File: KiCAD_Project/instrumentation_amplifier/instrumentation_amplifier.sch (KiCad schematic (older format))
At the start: 29 parts, among them CON1 1-0000001, J1 1-0000120, J2 Jumper, J3 Jumper, J4 1-0000120, SW1 1-0000852, U1 1-0000801, U2 1-0000465

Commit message: Production ready Rev 1.0
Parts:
- added J5: NP_Conn_01x04, np_connectors:PinHeader_1x04_P2.54mm_Vertical, symbol np_connectors:NP_Conn_01x04
- added PCB1: barepcb, misc:barepcb, symbol misc:barepcb
- FID1, FID2: footprint Fiducial:Fiducial_0.5mm_Mask1.5mm -> mechanical:Fiducial_1mm_Mask2mm; symbol Mechanical:Fiducial -> mechanical:Fiducial_1mm_2mm; Internal Part Number (none) -> 0-0000000; PValue (none) -> Fiducial; Populated (none) -> 0
- H1, H2, H3, H4: footprint MountingHole:MountingHole_2.1mm -> mechanical:MountingHole_3.2mm_M3_ISO7380; symbol Mechanical:MountingHole -> mechanical:M3_ISO_7380; Internal Part Number (none) -> 0-0000000; PValue (none) -> M3; Populated (none) -> 0
- J1: footprint capacitors_1206:1-0000191 -> connectors:1-0000120
- J2, J3: Internal Part Number (none) -> 0-0000000; Populated (none) -> 0
- R6: PValue 0R0 -> NP; Populated NP -> 0
- U1: symbol instrumentation_amplifier-rescue:1-0000801-amplifiers -> amplifiers:1-0000801
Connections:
- wire segments 80 -> 84
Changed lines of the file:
@@
 encoding utf-8
 Sheet 1 1
-Title "GEARS Instrumentation Amplifier"
-Date "2021-04-14"
+Title "Instrumentation Amplifier Demo"
+Date "2021-04-21"
 Rev "1.0"
 Comp "Leeman Geophysical LLC"
@@
 $EndComp
 $Comp
-L instrumentation_amplifier-rescue:1-0000801-amplifiers U1
+L amplifiers:1-0000801 U1
 U 1 1 60778415
 P 6700 3825
@@
 F 3 "~" H 4550 4450 50  0001 C CNN
 F 4 "1-0000006" H 4550 4450 50  0001 C CNN "Internal Part Number"
-F 5 "NP" H 4550 4450 50  0001 C CNN "Populated"
-F 6 "0R0" V 4550 4375 50  0000 L CNN "PValue"
+F 5 "0" H 4550 4450 50  0001 C CNN "Populated"
+F 6 "NP" V 4550 4400 50  0000 L CNN "PValue"
 	1    4550 4450
 	1    0    0    -1
@@
 F 0 "J1" H 3875 3675 50  0000 C CNN
 F 1 "1-0000120" H 3875 3675 50  0001 C CNN
-F 2 "capacitors_1206:1-0000191" H 3875 3875 50  0001 C CNN
+F 2 "connectors:1-0000120" H 3875 3875 50  0001 C CNN
 F 3 "~" H 3875 3875 50  0001 C CNN
 F 4 "1-0000120" H 3875 3875 50  0001 C CNN "Internal Part Number"
 F 5 "1" H 3875 3875 50  0001 C CNN "Populated"
-F 6 "TSW-102-07-T-S" H 3875 3575 50  0000 C CNN "PValue"
+F 6 "TSW-102-07-T-S" H 3875 3575 50  0001 C CNN "PValue"
 	1    3875 3875
 	-1   0    0    1
@@
 F 4 "1-0000120" H 8475 3825 50  0001 C CNN "Internal Part Number"
 F 5 "1" H 8475 3825 50  0001 C CNN "Populated"
-F 6 "TSW-102-07-T-S" H 8475 4025 50  0000 C CNN "PValue"
+F 6 "TSW-102-07-T-S" H 8475 4025 50  0001 C CNN "PValue"
 	1    8475 3825
 	1    0    0    -1
@@
 U 1 1 607ABDFA
 P 4425 2600
-F 0 "J3" V 4429 2680 50  0000 L CNN
-F 1 "Jumper" V 4520 2680 50  0000 L CNN
+F 0 "J3" V 4425 2325 50  0000 L CNN
+F 1 "Jumper" V 4525 2150 50  0000 L CNN
 F 2 "Connector_PinHeader_2.54mm:PinHeader_2x02_P2.54mm_Vertical" H 4425 2600 50  0001 C CNN
 F 3 "~" H 4425 2600 50  0001 C CNN
+F 4 "0-0000000" H 4425 2600 50  0001 C CNN "Internal Part Number"
+F 5 "0" H 4425 2600 50  0001 C CNN "Populated"
 	1    4425 2600
 	0    1    1    0
@@
 F 2 "Connector_PinHeader_2.54mm:PinHeader_2x02_P2.54mm_Vertical" H 4325 5125 50  0001 C CNN
 F 3 "~" H 4325 5125 50  0001 C CNN
+F 4 "0-0000000" H 4325 5125 50  0001 C CNN "Internal Part Number"
+F 5 "0" H 4325 5125 50  0001 C CNN "Populated"
 	1    4325 5125
 	0    -1   -1   0
@@
 $EndComp
 $Comp
-L Mechanical:MountingHole H1
+L mechanical:M3_ISO_7380 H1
 U 1 1 60869A6E
 P 700 6825
 F 0 "H1" H 800 6871 50  0000 L CNN
 F 1 "MountingHole" H 800 6780 50  0000 L CNN
-F 2 "MountingHole:MountingHole_2.1mm" H 700 6825 50  0001 C CNN
-F 3 "~" H 700 6825 50  0001 C CNN
+F 2 "mechanical:MountingHole_3.2mm_M3_ISO7380" H 700 6825 50  0001 C CNN
+F 3 "None" H 700 6825 50  0001 C CNN
+F 4 "0-0000000" H 700 6825 50  0001 C CNN "Internal Part Number"
+F 5 "0" H 700 6825 50  0001 C CNN "Populated"
+F 6 "M3" H 700 6825 50  0001 C CNN "PValue"
 	1    700  6825
 	1    0    0    -1
 $EndComp
 $Comp
-L Mechanical:MountingHole H2
+L mechanical:M3_ISO_7380 H2
 U 1 1 6086A8C6
 P 700 7075
 F 0 "H2" H 800 7121 50  0000 L CNN
 F 1 "MountingHole" H 800 7030 50  0000 L CNN
-F 2 "MountingHole:MountingHole_2.1mm" H 700 7075 50  0001 C CNN
-F 3 "~" H 700 7075 50  0001 C CNN
+F 2 "mechanical:MountingHole_3.2mm_M3_ISO7380" H 700 7075 50  0001 C CNN
+F 3 "None" H 700 7075 50  0001 C CNN
+F 4 "0-0000000" H 700 7075 50  0001 C CNN "Internal Part Number"
+F 5 "0" H 700 7075 50  0001 C CNN "Populated"
+F 6 "M3" H 700 7075 50  0001 C CNN "PValue"
 	1    700  7075
 	1    0    0    -1
 $EndComp
 $Comp
-L Mechanical:MountingHole H3
+L mechanical:M3_ISO_7380 H3
 U 1 1 6086B2CF
 P 700 7325
 F 0 "H3" H 800 7371 50  0000 L CNN
 F 1 "MountingHole" H 800 7280 50  0000 L CNN
-F 2 "MountingHole:MountingHole_2.1mm" H 700 7325 50  0001 C CNN
-F 3 "~" H 700 7325 50  0001 C CNN
+F 2 "mechanical:MountingHole_3.2mm_M3_ISO7380" H 700 7325 50  0001 C CNN
+F 3 "None" H 700 7325 50  0001 C CNN
+F 4 "0-0000000" H 700 7325 50  0001 C CNN "Internal Part Number"
+F 5 "0" H 700 7325 50  0001 C CNN "Populated"
+F 6 "M3" H 700 7325 50  0001 C CNN "PValue"
 	1    700  7325
 	1    0    0    -1
 $EndComp
 $Comp
-L Mechanical:MountingHole H4
+L mechanical:M3_ISO_7380 H4
 U 1 1 6086D5E1
 P 700 7575
 F 0 "H4" H 800 7621 50  0000 L CNN
 F 1 "MountingHole" H 800 7530 50  0000 L CNN
-F 2 "MountingHole:MountingHole_2.1mm" H 700 7575 50  0001 C CNN
-F 3 "~" H 700 7575 50  0001 C CNN
+F 2 "mechanical:MountingHole_3.2mm_M3_ISO7380" H 700 7575 50  0001 C CNN
+F 3 "None" H 700 7575 50  0001 C CNN
+F 4 "0-0000000" H 700 7575 50  0001 C CNN "Internal Part Number"
+F 5 "0" H 700 7575 50  0001 C CNN "Populated"
+F 6 "M3" H 700 7575 50  0001 C CNN "PValue"
 	1    700  7575
 	1    0    0    -1
@@
 	6700 2750 6700 3125
 $Comp
-L Mechanical:Fiducial FID1
+L mechanical:Fiducial_1mm_2mm FID1
 U 1 1 607C3F0B
 P 1575 6825
 F 0 "FID1" H 1660 6871 50  0000 L CNN
 F 1 "Fiducial" H 1660 6780 50  0000 L CNN
-F 2 "Fiducial:Fiducial_0.5mm_Mask1.5mm" H 1575 6825 50  0001 C CNN
+F 2 "mechanical:Fiducial_1mm_Mask2mm" H 1575 6825 50  0001 C CNN
 F 3 "~" H 1575 6825 50  0001 C CNN
+F 4 "0-0000000" H 1575 6825 50  0001 C CNN "Internal Part Number"
+F 5 "0" H 1575 6825 50  0001 C CNN "Populated"
+F 6 "Fiducial" H 1575 6825 50  0001 C CNN "PValue"
 	1    1575 6825
 	1    0    0    -1
 $EndComp
 $Comp
-L Mechanical:Fiducial FID2
+L mechanical:Fiducial_1mm_2mm FID2
 U 1 1 607C4B56
 P 1575 7100
 F 0 "FID2" H 1660 7146 50  0000 L CNN
 F 1 "Fiducial" H 1660 7055 50  0000 L CNN
-F 2 "Fiducial:Fiducial_0.5mm_Mask1.5mm" H 1575 7100 50  0001 C CNN
+F 2 "mechanical:Fiducial_1mm_Mask2mm" H 1575 7100 50  0001 C CNN
 F 3 "~" H 1575 7100 50  0001 C CNN
+F 4 "0-0000000" H 1575 7100 50  0001 C CNN "Internal Part Number"
+F 5 "0" H 1575 7100 50  0001 C CNN "Populated"
+F 6 "Fiducial" H 1575 7100 50  0001 C CNN "PValue"
 	1    1575 7100
 	1    0    0    -1
 $EndComp
+$Comp
+L power:+5V #PWR0113
+U 1 1 60809472
+P -600 1300
+F 0 "#PWR0113" H -600 1150 50  0001 C CNN
+F 1 "+5V" H -585 1473 50  0000 C CNN
+F 2 "" H -600 1300 50  0001 C CNN
+F 3 "" H -600 1300 50  0001 C CNN
+	1    -600 1300
+	1    0    0    -1
+$EndComp
+$Comp
+L power:-5V #PWR0114
+U 1 1 608096D5
+P -950 1300
+F 0 "#PWR0114" H -950 1400 50  0001 C CNN
+F 1 "-5V" H -935 1473 50  0000 C CNN
+F 2 "" H -950 1300 50  0001 C CNN
+F 3 "" H -950 1300 50  0001 C CNN
+	1    -950 1300
+	-1   0    0    1
+$EndComp
+$Comp
+L power:GND #PWR0115
+U 1 1 60809941
+P -1350 1300
+F 0 "#PWR0115" H -1350 1050 50  0001 C CNN
+F 1 "GND" H -1345 1127 50  0000 C CNN
+F 2 "" H -1350 1300 50  0001 C CNN
+F 3 "" H -1350 1300 50  0001 C CNN
+	1    -1350 1300
+	1    0    0    -1
+$EndComp
+$Comp
+L power:PWR_FLAG #FLG0101
+U 1 1 60809C8F
+P -950 1300
+F 0 "#FLG0101" H -950 1375 50  0001 C CNN
+F 1 "PWR_FLAG" H -950 1473 50  0000 C CNN
+F 2 "" H -950 1300 50  0001 C CNN
+F 3 "~" H -950 1300 50  0001 C CNN
+	1    -950 1300
+	1    0    0    -1
+$EndComp
+$Comp
+L power:PWR_FLAG #FLG0102
+U 1 1 6080A993
+P -1350 1300
+F 0 "#FLG0102" H -1350 1375 50  0001 C CNN
+F 1 "PWR_FLAG" H -1350 1473 50  0000 C CNN
+F 2 "" H -1350 1300 50  0001 C CNN
+F 3 "~" H -1350 1300 50  0001 C CNN
+	1    -1350 1300
+	1    0    0    -1
+$EndComp
+$Comp
+L power:PWR_FLAG #FLG0103
+U 1 1 6080AF02
+P -600 1300
+F 0 "#FLG0103" H -600 1375 50  0001 C CNN
+F 1 "PWR_FLAG" H -600 1473 50  0000 C CNN
+F 2 "" H -600 1300 50  0001 C CNN
+F 3 "~" H -600 1300 50  0001 C CNN
+	1    -600 1300
+	-1   0    0    1
+$EndComp
+$Comp
+L misc:barepcb PCB1
+U 1 1 6081342E
+P 10600 6325
+F 0 "PCB1" H 10500 6375 50  0000 L CNN
+F 1 "barepcb" H 10450 6275 50  0000 L CNN
+F 2 "misc:barepcb" H 10600 6325 50  0001 C CNN
+F 3 "" H 10600 6325 50  0001 C CNN
+F 4 "3-0000082" H 10600 6325 50  0001 C CNN "Internal Part Number"
+F 5 "1" H 10600 6325 50  0001 C CNN "Populated"
+F 6 "Bare PCB" H 10600 6325 50  0001 C CNN "PValue"
+	1    10600 6325
+	1    0    0    -1
+$EndComp
+$Comp
+L np_connectors:NP_Conn_01x04 J5
+U 1 1 6081C83C
+P 2175 3875
+F 0 "J5" H 2255 3867 50  0000 L CNN
+F 1 "NP_Conn_01x04" H 2175 3575 50  0001 C CNN
+F 2 "np_connectors:PinHeader_1x04_P2.54mm_Vertical" H 2175 3875 50  0001 C CNN
+F 3 "~" H 2175 3875 50  0001 C CNN
+F 4 "0-0000000" H 2175 3875 50  0001 C CNN "Internal Part Number"
+F 5 "0" H 2175 3875 50  0001 C CNN "Populated"
+F 6 "Power" H 2255 3776 50  0000 L CNN "PValue"
+	1    2175 3875
+	1    0    0    -1
+$EndComp
+$Comp
+L power:-5V #PWR0116
+U 1 1 6081E16C
+P 1975 4075
+F 0 "#PWR0116" H 1975 4175 50  0001 C CNN
+F 1 "-5V" H 1990 4248 50  0000 C CNN
+F 2 "" H 1975 4075 50  0001 C CNN
+F 3 "" H 1975 4075 50  0001 C CNN
+	1    1975 4075
+	-1   0    0    1
+$EndComp
+$Comp
+L power:+5V #PWR0117
+U 1 1 6081E5EF
+P 1975 3775
+F 0 "#PWR0117" H 1975 3625 50  0001 C CNN
+F 1 "+5V" H 1990 3948 50  0000 C CNN
+F 2 "" H 1975 3775 50  0001 C CNN
+F 3 "" H 1975 3775 50  0001 C CNN
+	1    1975 3775
+	1    0    0    -1
+$EndComp
+$Comp
+L power:GND #PWR0118
+U 1 1 6081EBDE
+P 1725 4100
+F 0 "#PWR0118" H 1725 3850 50  0001 C CNN
+F 1 "GND" H 1730 3927 50  0000 C CNN
+F 2 "" H 1725 4100 50  0001 C CNN
+F 3 "" H 1725 4100 50  0001 C CNN
+	1    1725 4100
+	1    0    0    -1
+$EndComp
+Wire Wire Line
+	1725 4100 1725 3975
+Wire Wire Line
+	1725 3975 1975 3975
+Wire Wire Line
+	1975 3875 1725 3875
+Wire Wire Line
+	1725 3875 1725 3975
+Connection ~ 1725 3975
 $EndSCHEMATC

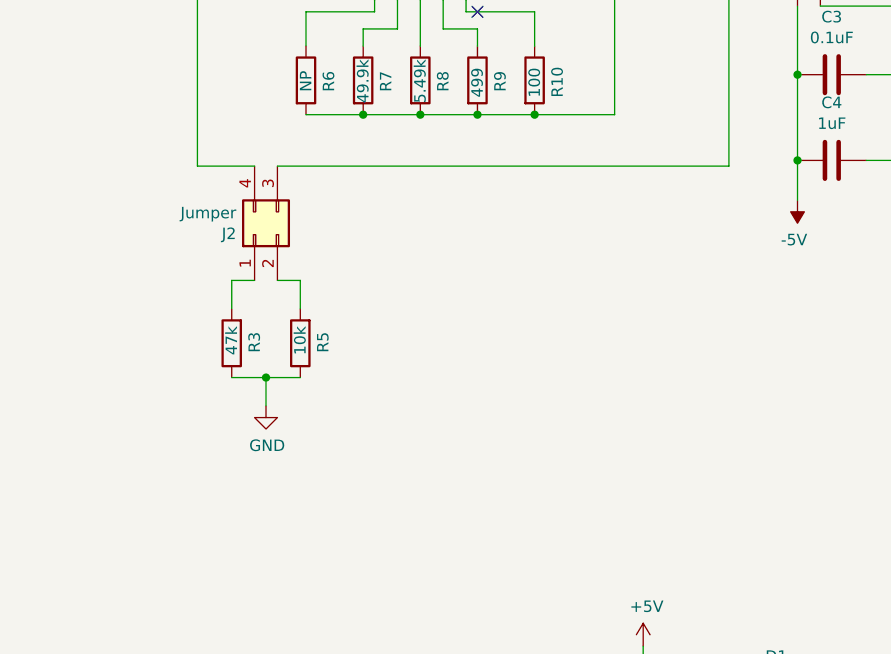
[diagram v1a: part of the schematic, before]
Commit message: Fixed schematic issue
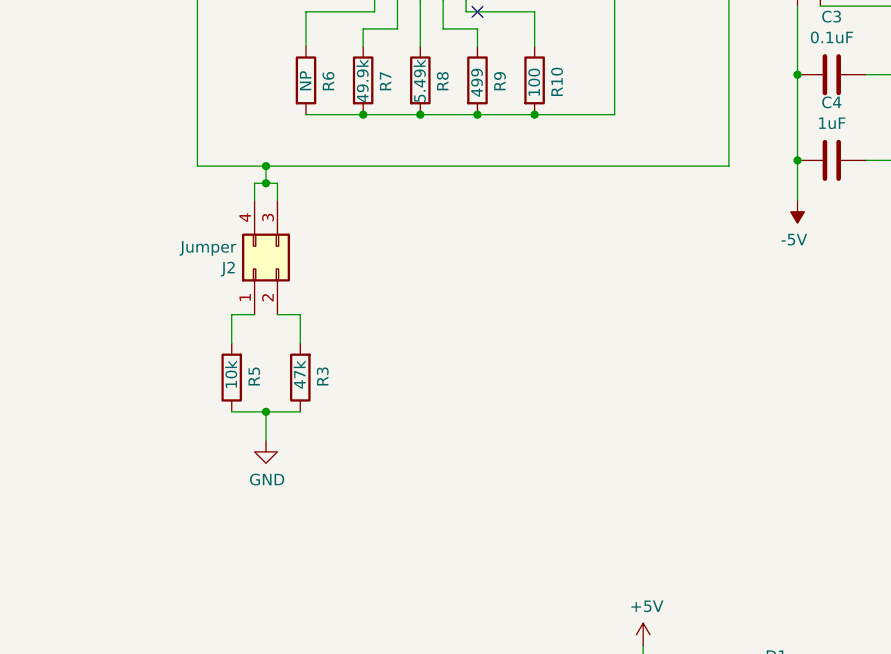
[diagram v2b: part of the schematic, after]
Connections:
- net at J2.3 (Pin_3), U1.2 (-): now also J1.1 (Pin_1), J2.4 (Pin_4)
- net at J2.1 (Pin_1): now also R5.2; no longer R3.2
- net at J2.2 (Pin_2): now also R3.2; no longer R5.2
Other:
- moved on the sheet: J2, R3, R5
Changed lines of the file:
@@
 	6400 4025 6400 4825
-Wire Wire Line
-	6400 4825 4425 4825
 Wire Wire Line
 	4075 4825 4075 3875
@@
 L Connector_Generic:Conn_02x02_Counter_Clockwise J2
 U 1 1 607C3542
-P 4325 5125
-F 0 "J2" V 4329 5205 50  0000 L CNN
-F 1 "Jumper" V 4420 5205 50  0000 L CNN
-F 2 "Connector_PinHeader_2.54mm:PinHeader_2x02_P2.54mm_Vertical" H 4325 5125 50  0001 C CNN
-F 3 "~" H 4325 5125 50  0001 C CNN
-F 4 "0-0000000" H 4325 5125 50  0001 C CNN "Internal Part Number"
-F 5 "0" H 4325 5125 50  0001 C CNN "Populated"
-	1    4325 5125
+P 4325 5275
+F 0 "J2" V 4329 5355 50  0000 L CNN
+F 1 "Jumper" V 4420 5355 50  0000 L CNN
+F 2 "Connector_PinHeader_2.54mm:PinHeader_2x02_P2.54mm_Vertical" H 4325 5275 50  0001 C CNN
+F 3 "~" H 4325 5275 50  0001 C CNN
+F 4 "0-0000000" H 4325 5275 50  0001 C CNN "Internal Part Number"
+F 5 "0" H 4325 5275 50  0001 C CNN "Populated"
+	1    4325 5275
 	0    -1   -1   0
 $EndComp
@@
 L resistors_0603:1-0000010 R5
 U 1 1 607C354B
-P 4525 5600
-F 0 "R5" V 4425 5550 50  0000 L CNN
-F 1 "1-0000010" V 4525 5600 50  0001 C CNN
-F 2 "resistors_0603:1-0000010" V 4455 5600 50  0001 C CNN
-F 3 "~" H 4525 5600 50  0001 C CNN
-F 4 "1-0000010" H 4525 5600 50  0001 C CNN "Internal Part Number"
-F 5 "1" H 4525 5600 50  0001 C CNN "Populated"
-F 6 "10k" V 4525 5525 50  0000 L CNN "PValue"
-	1    4525 5600
+P 4225 5750
+F 0 "R5" V 4125 5700 50  0000 L CNN
+F 1 "1-0000010" V 4225 5750 50  0001 C CNN
+F 2 "resistors_0603:1-0000010" V 4155 5750 50  0001 C CNN
+F 3 "~" H 4225 5750 50  0001 C CNN
+F 4 "1-0000010" H 4225 5750 50  0001 C CNN "Internal Part Number"
+F 5 "1" H 4225 5750 50  0001 C CNN "Populated"
+F 6 "10k" V 4225 5675 50  0000 L CNN "PValue"
+	1    4225 5750
 	-1   0    0    1
 $EndComp
@@
 L resistors_0603:1-0000011 R3
 U 1 1 607C3554
-P 4225 5600
-F 0 "R3" V 4125 5550 50  0000 L CNN
-F 1 "1-0000011" V 4225 5600 50  0001 C CNN
-F 2 "resistors_0603:1-0000011" V 4155 5600 50  0001 C CNN
-F 3 "~" H 4225 5600 50  0001 C CNN
-F 4 "1-0000011" H 4225 5600 50  0001 C CNN "Internal Part Number"
-F 5 "1" H 4225 5600 50  0001 C CNN "Populated"
-F 6 "47k" V 4225 5525 50  0000 L CNN "PValue"
-	1    4225 5600
-	-1   0    0    1
-$EndComp
-Wire Wire Line
-	4525 5450 4525 5325
-Wire Wire Line
-	4525 5325 4425 5325
-Wire Wire Line
-	4225 5450 4225 5325
-Wire Wire Line
-	4225 5325 4325 5325
+P 4525 5750
+F 0 "R3" V 4425 5700 50  0000 L CNN
+F 1 "1-0000011" V 4525 5750 50  0001 C CNN
+F 2 "resistors_0603:1-0000011" V 4455 5750 50  0001 C CNN
+F 3 "~" H 4525 5750 50  0001 C CNN
+F 4 "1-0000011" H 4525 5750 50  0001 C CNN "Internal Part Number"
+F 5 "1" H 4525 5750 50  0001 C CNN "Populated"
+F 6 "47k" V 4525 5675 50  0000 L CNN "PValue"
+	1    4525 5750
+	-1   0    0    1
+$EndComp
+Wire Wire Line
+	4525 5600 4525 5475
+Wire Wire Line
+	4525 5475 4425 5475
+Wire Wire Line
+	4225 5600 4225 5475
+Wire Wire Line
+	4225 5475 4325 5475
 $Comp
 L power:GND #PWR0107
 U 1 1 607C3561
-P 4375 5875
-F 0 "#PWR0107" H 4375 5625 50  0001 C CNN
-F 1 "GND" H 4380 5702 50  0000 C CNN
-F 2 "" H 4375 5875 50  0001 C CNN
-F 3 "" H 4375 5875 50  0001 C CNN
-	1    4375 5875
-	1    0    0    -1
-$EndComp
-Wire Wire Line
-	4225 5750 4375 5750
-Wire Wire Line
-	4375 5750 4375 5875
-Connection ~ 4375 5750
-Wire Wire Line
-	4375 5750 4525 5750
-Wire Wire Line
-	4325 4825 4075 4825
+P 4375 6025
+F 0 "#PWR0107" H 4375 5775 50  0001 C CNN
+F 1 "GND" H 4380 5852 50  0000 C CNN
+F 2 "" H 4375 6025 50  0001 C CNN
+F 3 "" H 4375 6025 50  0001 C CNN
+	1    4375 6025
+	1    0    0    -1
+$EndComp
+Wire Wire Line
+	4225 5900 4375 5900
+Wire Wire Line
+	4375 5900 4375 6025
+Connection ~ 4375 5900
+Wire Wire Line
+	4375 5900 4525 5900
 Wire Wire Line
 	6025 6925 6025 7225
@@
 	1725 3875 1725 3975
 Connection ~ 1725 3975
+Wire Wire Line
+	4425 4975 4425 4900
+Wire Wire Line
+	4425 4900 4375 4900
+Wire Wire Line
+	4325 4900 4325 4975
+Wire Wire Line
+	4375 4900 4375 4825
+Connection ~ 4375 4900
+Wire Wire Line
+	4375 4900 4325 4900
+Wire Wire Line
+	4075 4825 4375 4825
+Wire Wire Line
+	4375 4825 6400 4825
+Connection ~ 4375 4825
 $EndSCHEMATC

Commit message: Rev 1.1 Production
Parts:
- PCB1: Internal Part Number 3-0000082 -> 3-0000087
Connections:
- no-connect marks 2 -> 1
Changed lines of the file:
@@
 Sheet 1 1
 Title "Instrumentation Amplifier Demo"
-Date "2021-04-21"
-Rev "1.0"
+Date "2021-05-11"
+Rev "1.1"
 Comp "Leeman Geophysical LLC"
 Comment1 "(479) 373-3736"
@@
 	1    0    0    -1
 $EndComp
-NoConn ~ 5300 4150
 $Comp
 L dc_dc_converters:1-0000465 U2
@@
 F 2 "misc:barepcb" H 10600 6325 50  0001 C CNN
 F 3 "" H 10600 6325 50  0001 C CNN
-F 4 "3-0000082" H 10600 6325 50  0001 C CNN "Internal Part Number"
+F 4 "3-0000087" H 10600 6325 50  0001 C CNN "Internal Part Number"
 F 5 "1" H 10600 6325 50  0001 C CNN "Populated"
 F 6 "Bare PCB" H 10600 6325 50  0001 C CNN "PValue"
